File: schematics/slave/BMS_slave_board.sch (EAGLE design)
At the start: 62 parts, among them IC2 LT1021S, J1 AVR_SPI_PRG_6NS, Q1 BUZ10, Q2 BUZ10, Q3 BUZ10, Q4 BUZ10, U1 LMV324, U2 LMV324

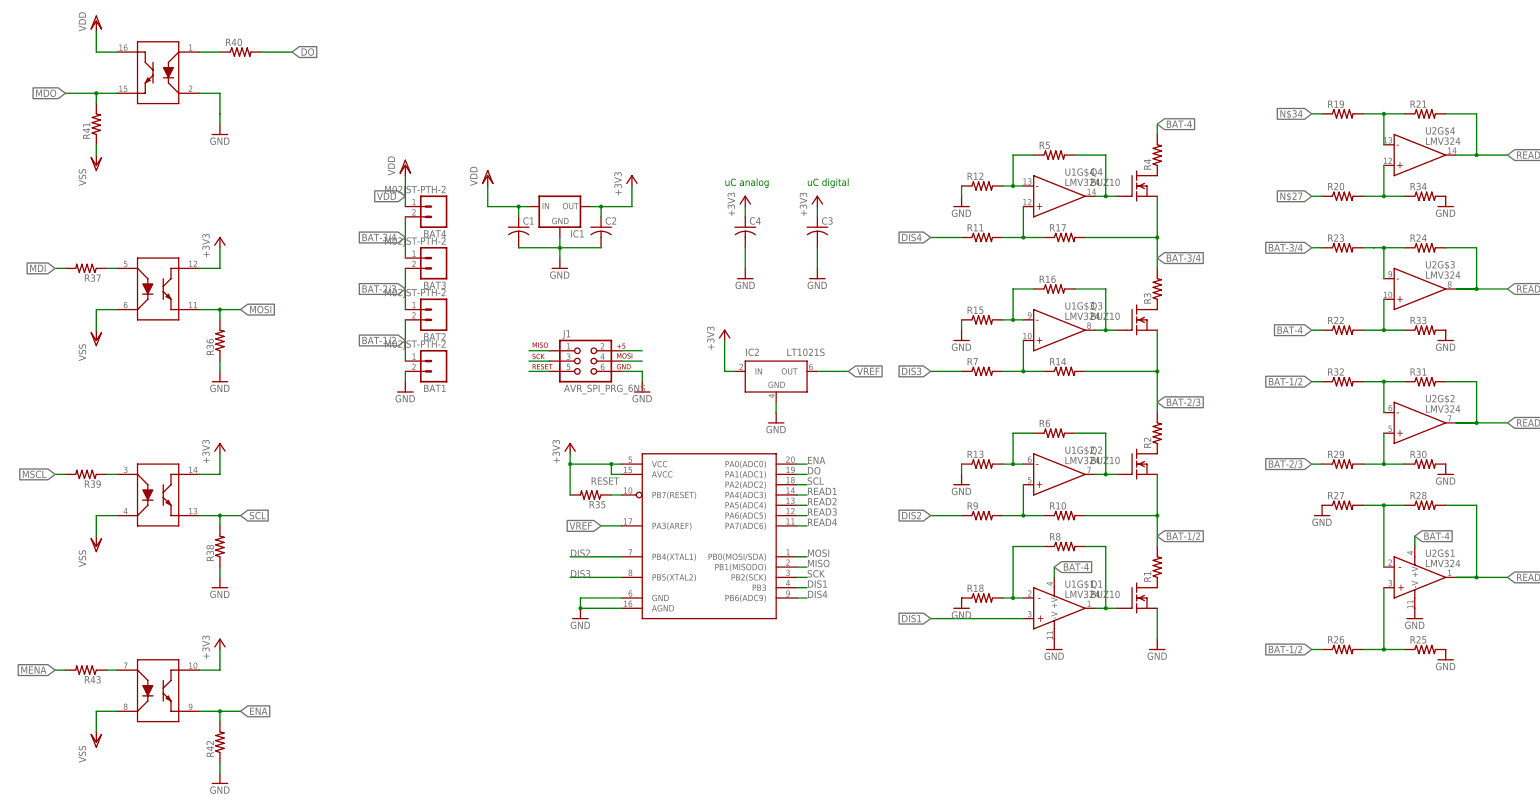
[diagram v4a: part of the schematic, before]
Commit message: modified power supplies
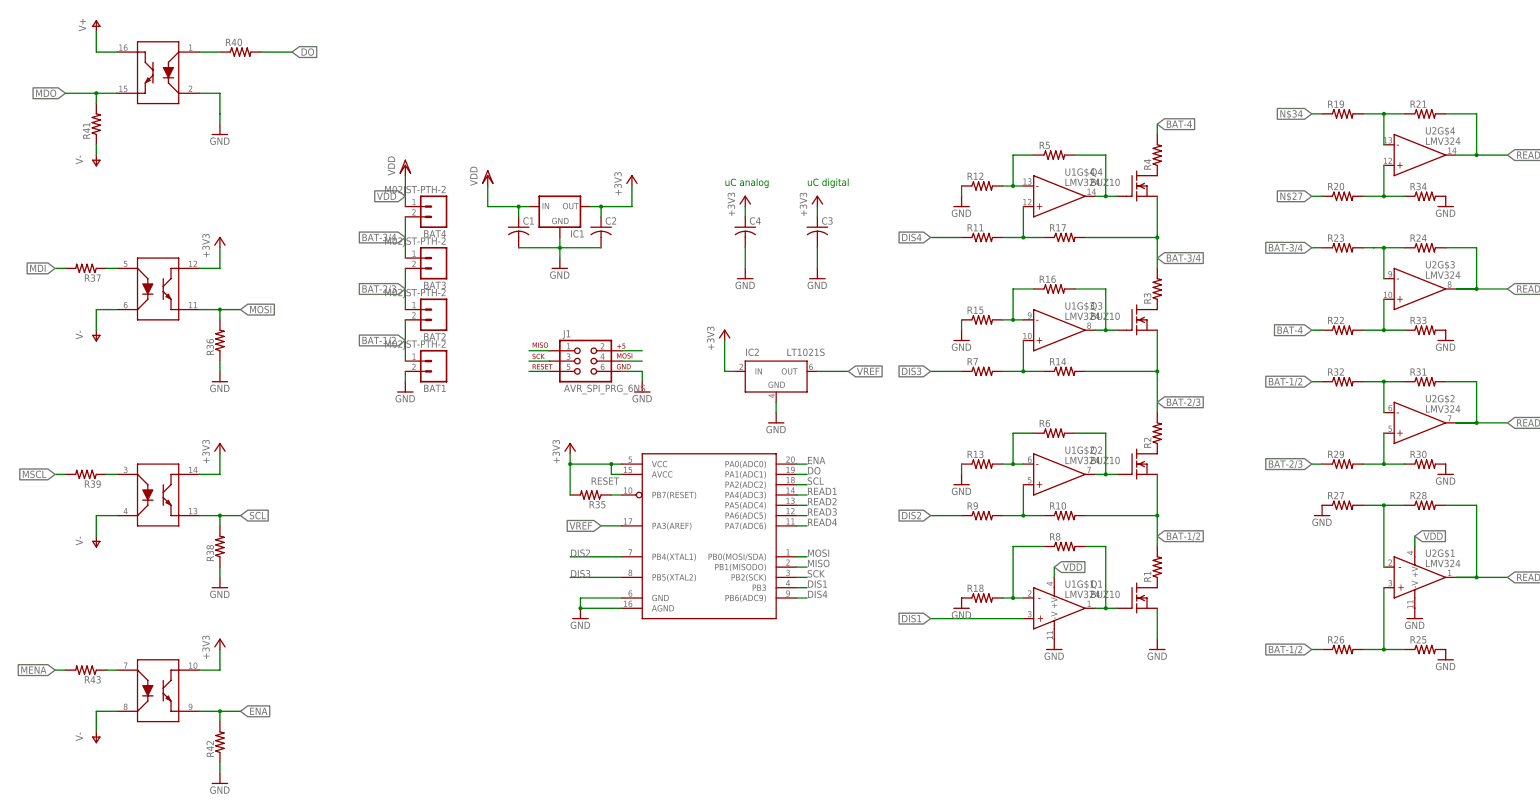
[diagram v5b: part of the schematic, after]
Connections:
- net VSS renamed V-
- new net V+: U$2G$1.CO
- net BAT-4: no longer U1G$1.+V, U2G$1.+V
- net VDD: now also U1G$1.+V, U2G$1.+V; no longer U$2G$1.CO
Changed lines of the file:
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@@
 <part name="R40" library="rcl" deviceset="R-US_" device="0204/7"/>
 <part name="R41" library="rcl" deviceset="R-US_" device="0204/7"/>
-<part name="VSS1" library="supply1" deviceset="VSS" device=""/>
-<part name="VSS2" library="supply1" deviceset="VSS" device=""/>
 <part name="+3V6" library="supply1" deviceset="+3V3" device=""/>
 <part name="R38" library="rcl" deviceset="R-US_" device="0204/7"/>
 <part name="GND21" library="supply1" deviceset="GND" device=""/>
 <part name="R39" library="rcl" deviceset="R-US_" device="0204/7"/>
-<part name="VSS3" library="supply1" deviceset="VSS" device=""/>
 <part name="+3V8" library="supply1" deviceset="+3V3" device=""/>
 <part name="R42" library="rcl" deviceset="R-US_" device="0204/7"/>
 <part name="GND22" library="supply1" deviceset="GND" device=""/>
 <part name="R43" library="rcl" deviceset="R-US_" device="0204/7"/>
-<part name="VSS4" library="supply1" deviceset="VSS" device=""/>
 <part name="GND23" library="supply1" deviceset="GND" device=""/>
-<part name="VDD3" library="supply1" deviceset="VDD" device=""/>
+<part name="P+1" library="supply1" deviceset="V+" device=""/>
+<part name="P-1" library="supply1" deviceset="V-" device=""/>
+<part name="P-2" library="supply1" deviceset="V-" device=""/>
+<part name="P-3" library="supply1" deviceset="V-" device=""/>
+<part name="P-4" library="supply1" deviceset="V-" device=""/>
 </parts>
 <sheets>
@@
 <instance part="R40" gate="G$1" x="-149.86" y="152.4"/>
 <instance part="R41" gate="G$1" x="-185.42" y="134.62" rot="R90"/>
-<instance part="VSS1" gate="G$1" x="-185.42" y="124.46"/>
-<instance part="VSS2" gate="G$1" x="-185.42" y="81.28"/>
 <instance part="+3V6" gate="G$1" x="-154.94" y="55.88"/>
 <instance part="R38" gate="G$1" x="-154.94" y="30.48" rot="R90"/>
 <instance part="GND21" gate="1" x="-154.94" y="20.32"/>
 <instance part="R39" gate="G$1" x="-187.96" y="48.26" rot="R180"/>
-<instance part="VSS3" gate="G$1" x="-185.42" y="30.48"/>
 <instance part="+3V8" gate="G$1" x="-154.94" y="7.62"/>
 <instance part="R42" gate="G$1" x="-154.94" y="-17.78" rot="R90"/>
 <instance part="GND22" gate="1" x="-154.94" y="-27.94"/>
 <instance part="R43" gate="G$1" x="-187.96" y="0" rot="R180"/>
-<instance part="VSS4" gate="G$1" x="-185.42" y="-17.78"/>
 <instance part="U$2" gate="G$2" x="-170.18" y="43.18" rot="R270"/>
 <instance part="U$2" gate="G$4" x="-170.18" y="-5.08" rot="R270"/>
 <instance part="GND23" gate="1" x="-154.94" y="132.08"/>
-<instance part="VDD3" gate="G$1" x="-185.42" y="160.02"/>
+<instance part="P+1" gate="1" x="-185.42" y="160.02"/>
+<instance part="P-1" gate="1" x="-185.42" y="124.46"/>
+<instance part="P-2" gate="1" x="-185.42" y="81.28"/>
+<instance part="P-3" gate="1" x="-185.42" y="30.48"/>
+<instance part="P-4" gate="1" x="-185.42" y="-17.78"/>
 </instances>
 <busses>
@@
 <net name="BAT-4" class="0">
 <segment>
-<pinref part="U1" gate="G$1" pin="+V"/>
-<wire x1="50.8" y1="22.86" x2="50.8" y2="25.4" width="0.1524" layer="91"/>
-<label x="50.8" y="25.4" size="1.778" layer="95" xref="yes"/>
-</segment>
-<segment>
 <pinref part="R4" gate="G$1" pin="2"/>
 <wire x1="76.2" y1="132.08" x2="76.2" y2="134.62" width="0.1524" layer="91"/>
 <label x="76.2" y="134.62" size="1.778" layer="95" xref="yes"/>
-</segment>
-<segment>
-<pinref part="U2" gate="G$1" pin="+V"/>
-<wire x1="139.7" y1="30.48" x2="139.7" y2="33.02" width="0.1524" layer="91"/>
-<label x="139.7" y="33.02" size="1.778" layer="95" xref="yes"/>
 </segment>
 <segment>
@@
 </segment>
 <segment>
-<pinref part="U$2" gate="G$1" pin="CO"/>
-<wire x1="-180.34" y1="152.4" x2="-185.42" y2="152.4" width="0.1524" layer="91"/>
-<wire x1="-185.42" y1="152.4" x2="-185.42" y2="157.48" width="0.1524" layer="91"/>
-<pinref part="VDD3" gate="G$1" pin="VDD"/>
+<pinref part="U2" gate="G$1" pin="+V"/>
+<wire x1="139.7" y1="30.48" x2="139.7" y2="33.02" width="0.1524" layer="91"/>
+<label x="139.7" y="33.02" size="1.778" layer="95" xref="yes"/>
+</segment>
+<segment>
+<pinref part="U1" gate="G$1" pin="+V"/>
+<wire x1="50.8" y1="22.86" x2="50.8" y2="25.4" width="0.1524" layer="91"/>
+<label x="50.8" y="25.4" size="1.778" layer="95" xref="yes"/>
 </segment>
 </net>
@@
 </segment>
 </net>
-<net name="VSS" class="0">
-<segment>
-<pinref part="R41" gate="G$1" pin="1"/>
-<pinref part="VSS1" gate="G$1" pin="VSS"/>
-<wire x1="-185.42" y1="129.54" x2="-185.42" y2="127" width="0.1524" layer="91"/>
-</segment>
-<segment>
-<pinref part="U$2" gate="G$3" pin="CA"/>
-<pinref part="VSS2" gate="G$1" pin="VSS"/>
-<wire x1="-180.34" y1="88.9" x2="-185.42" y2="88.9" width="0.1524" layer="91"/>
-<wire x1="-185.42" y1="88.9" x2="-185.42" y2="83.82" width="0.1524" layer="91"/>
-</segment>
-<segment>
-<pinref part="VSS3" gate="G$1" pin="VSS"/>
-<wire x1="-180.34" y1="38.1" x2="-185.42" y2="38.1" width="0.1524" layer="91"/>
-<wire x1="-185.42" y1="38.1" x2="-185.42" y2="33.02" width="0.1524" layer="91"/>
-<pinref part="U$2" gate="G$2" pin="CA"/>
-</segment>
-<segment>
-<pinref part="VSS4" gate="G$1" pin="VSS"/>
-<wire x1="-180.34" y1="-10.16" x2="-185.42" y2="-10.16" width="0.1524" layer="91"/>
-<wire x1="-185.42" y1="-10.16" x2="-185.42" y2="-15.24" width="0.1524" layer="91"/>
-<pinref part="U$2" gate="G$4" pin="CA"/>
-</segment>
-</net>
 <net name="SCL" class="0">
 <segment>
@@
 </segment>
 </net>
+<net name="V+" class="0">
+<segment>
+<pinref part="U$2" gate="G$1" pin="CO"/>
+<wire x1="-180.34" y1="152.4" x2="-185.42" y2="152.4" width="0.1524" layer="91"/>
+<wire x1="-185.42" y1="152.4" x2="-185.42" y2="157.48" width="0.1524" layer="91"/>
+<pinref part="P+1" gate="1" pin="V+"/>
+</segment>
+</net>
+<net name="V-" class="0">
+<segment>
+<pinref part="R41" gate="G$1" pin="1"/>
+<wire x1="-185.42" y1="129.54" x2="-185.42" y2="127" width="0.1524" layer="91"/>
+<pinref part="P-1" gate="1" pin="V-"/>
+</segment>
+<segment>
+<pinref part="U$2" gate="G$3" pin="CA"/>
+<wire x1="-180.34" y1="88.9" x2="-185.42" y2="88.9" width="0.1524" layer="91"/>
+<wire x1="-185.42" y1="88.9" x2="-185.42" y2="83.82" width="0.1524" layer="91"/>
+<pinref part="P-2" gate="1" pin="V-"/>
+</segment>
+<segment>
+<wire x1="-180.34" y1="38.1" x2="-185.42" y2="38.1" width="0.1524" layer="91"/>
+<wire x1="-185.42" y1="38.1" x2="-185.42" y2="33.02" width="0.1524" layer="91"/>
+<pinref part="U$2" gate="G$2" pin="CA"/>
+<pinref part="P-3" gate="1" pin="V-"/>
+</segment>
+<segment>
+<wire x1="-180.34" y1="-10.16" x2="-185.42" y2="-10.16" width="0.1524" layer="91"/>
+<pinref part="U$2" gate="G$4" pin="CA"/>
+<wire x1="-185.42" y1="-10.16" x2="-185.42" y2="-15.24" width="0.1524" layer="91"/>
+<pinref part="P-4" gate="1" pin="V-"/>
+</segment>
+</net>

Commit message: innitial layout
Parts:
- removed BAT1, BAT2, BAT3, BAT4: M02JST-PTH-2, SparkFun-Connectors:M02JST-PTH-2
- removed IC1: (no value), v-reg:78LXX
- added B1, B1/2, B2/3, B3/4, B4: (no value), wirepad:2,15/1,0
- added IC3: 78L05F, linear:78L05F
- added X1, X2: 87438-05, con-molex:87438-05
- Q1, Q2, Q3, Q4: value BUZ10 -> BSS123; device transistor-fet:BUZ10 -> transistor-small-signal:BSS123
- R1, R10, R11, R12, R13, R14, R15, R16, R17, R18, R2, R20, R21, R22, R23, R24, R25, R26, R27, R28, R29, R3, R30, R31, R32, R33, R34, R35, R36, R37, R38, R39, R4, R40, R41, R42, R43, R5, R6, R7, R8, R9: device rcl:R-US_0204/7 -> rcl:R-US_R0603
- R19: device rcl:R-US_0204/7 -> rcl:R-US_M0805
- U$1: value ATTINY261ADIP -> ATTINY261ASOC; device EVT-Eagle-Library:ATTINY261ADIP -> EVT-Eagle-Library:ATTINY261ASOC
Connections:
- net +3V3: now also IC3.VO; no longer IC1.OUT
- net BAT-1/2: now also B1/2.P; no longer BAT1.1, BAT2.2
- net BAT-2/3: now also B2/3.P, Q1.S; no longer BAT2.1, BAT3.2, Q3.S
- net BAT-3/4: now also B3/4.P, Q3.S; no longer BAT3.1, BAT4.2, Q4.S
- net BAT-4: now also B4.P, U1G$1.+V, U2G$1.+V
- net GND: now also B1.P, IC3.GND, IC3.GND@1, Q4.S; no longer BAT1.2, IC1.GND, Q1.S
- net N$1: now also R3.1; no longer R1.1
- net N$33: now also Q3.G; no longer Q4.G
- net N$5: now also R4.1; no longer R3.1
- net N$7: now also R1.1; no longer R4.1
- net N$8: now also Q4.G; no longer Q1.G
- net N$9: now also Q1.G; no longer Q3.G
- net VDD: now also IC3.VI; no longer BAT4.1, IC1.IN, U1G$1.+V, U2G$1.+V
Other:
- moved on the sheet: C2
